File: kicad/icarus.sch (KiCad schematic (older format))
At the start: 78 parts, among them J1 CAN Bus, J2 CAN Bus, J3 SWD Programming, J4 USB_B_Micro, U1 MAX15062A, U10 XT30, U11 XT30, U12 XT30, U13 LT1787HVIMS8PBF, U14 USBLC6-2SC6, U15 STLM20DD9FUDFN-4L_STM-L, U2 STM32G474CEU6, U3 TCAN334G, U4 XT90, U5 FSV10150VTO277-3L_ONS-L, U6 XT30, U7 XT30, U8 TPS2490DGSR, U9 XT30

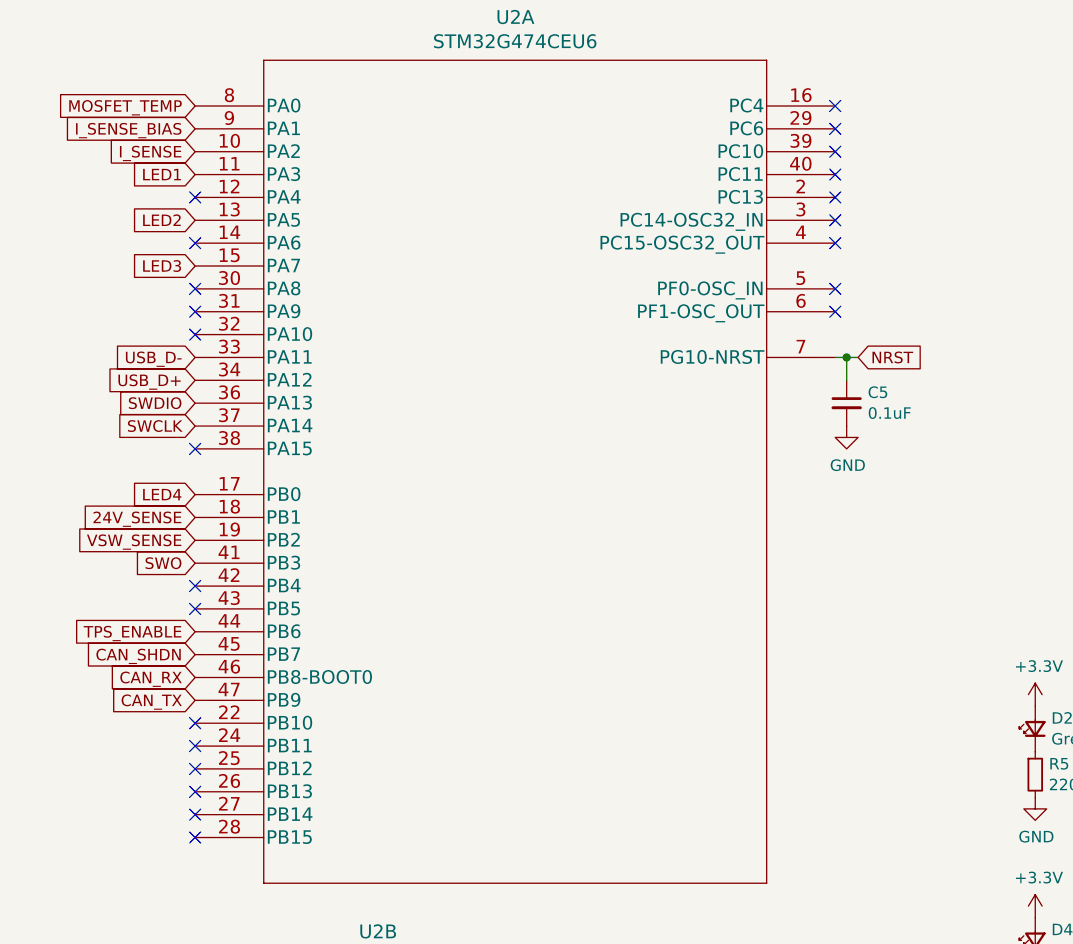
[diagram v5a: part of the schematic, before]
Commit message: Began initial routing
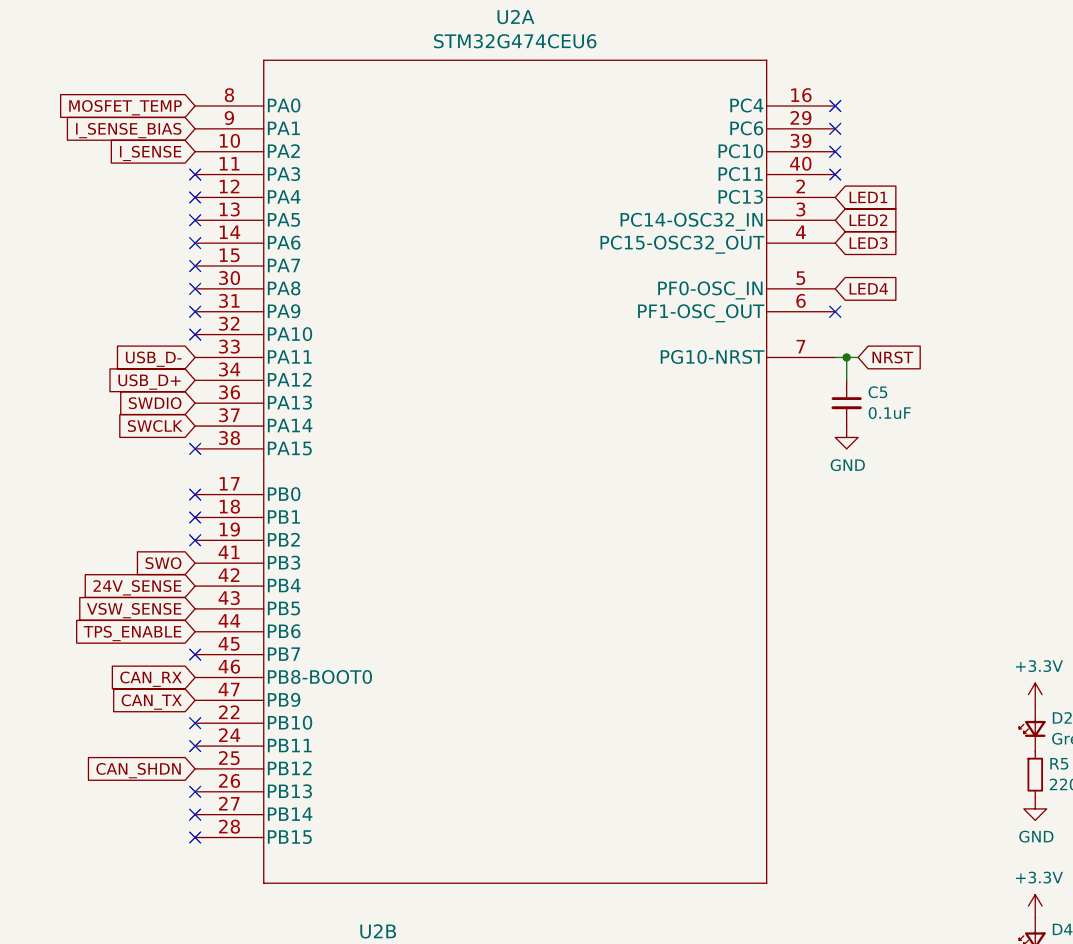
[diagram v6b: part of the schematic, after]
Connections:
- net 24V_SENSE: now also U2.42 (PB4); no longer U2.18 (PB1)
- net CAN_SHDN: now also U2.25 (PB12); no longer U2.45 (PB7)
- net LED1: now also U2.2 (PC13); no longer U2.11 (PA3)
- net LED2: now also U2.3 (PC14-OSC32_IN); no longer U2.13 (PA5)
- net LED3: now also U2.4 (PC15-OSC32_OUT); no longer U2.15 (PA7)
- net LED4: now also U2.5 (PF0-OSC_IN); no longer U2.17 (PB0)
- net VSW_SENSE: now also U2.43 (PB5); no longer U2.19 (PB2)
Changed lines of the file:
@@
 Text GLabel 1250 1625 0    50   Input ~ 0
 I_SENSE_BIAS
-Text GLabel 1250 3925 0    50   Input ~ 0
+Text GLabel 1250 4425 0    50   Input ~ 0
 CAN_SHDN
 $Comp
@@
 Wire Wire Line
 	8175 3525 8350 3525
-Text GLabel 1250 1825 0    50   Input ~ 0
+Text GLabel 4050 1925 2    50   Input ~ 0
 LED1
-Text GLabel 1250 2025 0    50   Input ~ 0
+Text GLabel 4050 2025 2    50   Input ~ 0
 LED2
 Text GLabel 1250 3825 0    50   Input ~ 0
@@
 Text GLabel 5500 6525 0    50   Input ~ 0
 LED4
-Text GLabel 1250 2225 0    50   Input ~ 0
+Text GLabel 4050 2125 2    50   Input ~ 0
 LED3
-Text GLabel 1250 3225 0    50   Input ~ 0
+Text GLabel 4050 2325 2    50   Input ~ 0
 LED4
 Wire Wire Line
@@
 Text GLabel 1250 1725 0    50   Input ~ 0
 I_SENSE
-Text GLabel 1250 3325 0    50   Input ~ 0
+Text GLabel 1250 3625 0    50   Input ~ 0
 24V_SENSE
-Text GLabel 1250 3425 0    50   Input ~ 0
+Text GLabel 1250 3725 0    50   Input ~ 0
 VSW_SENSE
 Text Notes 15425 5400 0    50   ~ 0
@@
 NoConn ~ 1250 2525
 NoConn ~ 1250 3025
-NoConn ~ 1250 3625
-NoConn ~ 1250 3725
 NoConn ~ 1250 4225
 NoConn ~ 1250 4325
-NoConn ~ 1250 4425
 NoConn ~ 1250 4525
 NoConn ~ 1250 4625
 NoConn ~ 1250 4725
 NoConn ~ 4050 2425
-NoConn ~ 4050 2325
-NoConn ~ 4050 2125
-NoConn ~ 4050 2025
-NoConn ~ 4050 1925
 NoConn ~ 4050 1825
 NoConn ~ 4050 1725
@@
 	1    0    0    -1
 $EndComp
+NoConn ~ 1250 3325
+NoConn ~ 1250 3425
+NoConn ~ 1250 3925
+NoConn ~ 1250 1825
+NoConn ~ 1250 2225
+NoConn ~ 1250 2025
+NoConn ~ 1250 3225
 $EndSCHEMATC

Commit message: Added ground plane, adjusted schematic
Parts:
- added JP1: Jumper_2_Bridged, icarus_kicad_lib:SHORT_TOP-BIG, symbol Jumper:Jumper_2_Bridged
- added R18: 6.8k, 1%, Resistor_SMD:R_0402_1005Metric, symbol Device:R_Small
- R17: value R_Small -> 6.8k, 1%
- renumbered R11 to R10, R12 to R11, R13 to R12, R14 to R13, R15 to R14, R2 to R15, R18 to R19, R3 to R2, R19 to R20, R20 to R21, R21 to R22, R4 to R3, R5 to R4, R6 to R5, R7 to R6, R8 to R7, R9 to R8, R10 to R9
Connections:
- net +3V3: now also R15.2
- net +VSW: no longer R15.2
- net GND: now also JP1.1 (A), R18.2; no longer C7.2, CR1.2, CR2.2, U10.-, U11.-, U12.-, U4.-, U5.1 (ANODE), U5.2 (ANODE_2), U6.-, U7.-, U9.-
- net I_SENSE: now also U2.9 (PA1); no longer U2.10 (PA2)
- net I_SENSE_BIAS: now also U2.10 (PA2); no longer U13.6 (VBIAS), U2.9 (PA1)
- net PG: now also U2.19 (PB2)
- net TPS_ENABLE: now also U2.24 (PB11); no longer U2.44 (PB6)
- net at C16.1, R17.2: now also U13.6 (VBIAS), R18.1
- new net GNDPWR: C7.2, CR1.2, CR2.2, JP1.2 (B), U10.-, U11.-, U12.-, U5.1 (ANODE), U5.2 (ANODE_2), U6.-, U7.-, U9.-
- no-connect marks 27 -> 26
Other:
- moved on the sheet: C16, R15

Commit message: Layout v1.0 done
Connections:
- net GND: no longer H2.1, H3.1
- net GNDPWR: now also U4.-
- no-connect marks 26 -> 28
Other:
- moved on the sheet: H2, H3, H4
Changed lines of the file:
@@
 L Mechanical:MountingHole_Pad H2
 U 1 1 604D92AD
+P 13275 6425
+F 0 "H2" V 13229 6575 50  0000 L CNN
+F 1 "MountingHole_Pad" V 13320 6575 50  0000 L CNN
+F 2 "MountingHole:MountingHole_2.7mm_M2.5_DIN965_Pad" H 13275 6425 50  0001 C CNN
+F 3 "~" H 13275 6425 50  0001 C CNN
+	1    13275 6425
+	0    1    1    0
+$EndComp
+$Comp
+L Mechanical:MountingHole_Pad H3
+U 1 1 604D9523
+P 13275 6625
+F 0 "H3" V 13229 6775 50  0000 L CNN
+F 1 "MountingHole_Pad" V 13320 6775 50  0000 L CNN
+F 2 "MountingHole:MountingHole_2.7mm_M2.5_DIN965_Pad" H 13275 6625 50  0001 C CNN
+F 3 "~" H 13275 6625 50  0001 C CNN
+	1    13275 6625
+	0    1    1    0
+$EndComp
+$Comp
+L Mechanical:MountingHole_Pad H4
+U 1 1 604D96CD
 P 13275 5975
-F 0 "H2" V 13229 6125 50  0000 L CNN
+F 0 "H4" V 13229 6125 50  0000 L CNN
 F 1 "MountingHole_Pad" V 13320 6125 50  0000 L CNN
 F 2 "MountingHole:MountingHole_2.7mm_M2.5_DIN965_Pad" H 13275 5975 50  0001 C CNN
@@
 $EndComp
 $Comp
-L Mechanical:MountingHole_Pad H3
-U 1 1 604D9523
-P 13275 6225
-F 0 "H3" V 13229 6375 50  0000 L CNN
-F 1 "MountingHole_Pad" V 13320 6375 50  0000 L CNN
-F 2 "MountingHole:MountingHole_2.7mm_M2.5_DIN965_Pad" H 13275 6225 50  0001 C CNN
-F 3 "~" H 13275 6225 50  0001 C CNN
-	1    13275 6225
-	0    1    1    0
-$EndComp
-$Comp
-L Mechanical:MountingHole_Pad H4
-U 1 1 604D96CD
-P 13275 6475
-F 0 "H4" V 13229 6625 50  0000 L CNN
-F 1 "MountingHole_Pad" V 13320 6625 50  0000 L CNN
-F 2 "MountingHole:MountingHole_2.7mm_M2.5_DIN965_Pad" H 13275 6475 50  0001 C CNN
-F 3 "~" H 13275 6475 50  0001 C CNN
-	1    13275 6475
-	0    1    1    0
-$EndComp
-$Comp
 L power:GND #PWR040
 U 1 1 604DA2B5
-P 13175 6600
-F 0 "#PWR040" H 13175 6350 50  0001 C CNN
-F 1 "GND" H 13180 6427 50  0000 C CNN
-F 2 "" H 13175 6600 50  0001 C CNN
-F 3 "" H 13175 6600 50  0001 C CNN
-	1    13175 6600
+P 13175 5975
+F 0 "#PWR040" H 13175 5725 50  0001 C CNN
+F 1 "GND" H 13180 5802 50  0000 C CNN
+F 2 "" H 13175 5975 50  0001 C CNN
+F 3 "" H 13175 5975 50  0001 C CNN
+	1    13175 5975
 	1    0    0    -1
 $EndComp
 Wire Wire Line
 	13175 5750 13175 5975
-Connection ~ 13175 5975
-Wire Wire Line
-	13175 5975 13175 6225
-Connection ~ 13175 6225
-Wire Wire Line
-	13175 6225 13175 6475
-Connection ~ 13175 6475
-Wire Wire Line
-	13175 6475 13175 6600
 $Comp
 L xt30:XT30 U6
@@
 Connection ~ 11625 3800
 $Comp
-L power:GNDPWR #PWR?
+L power:GNDPWR #PWR0105
 U 1 1 607A32D5
 P 11125 5600
-F 0 "#PWR?" H 11125 5400 50  0001 C CNN
+F 0 "#PWR0105" H 11125 5400 50  0001 C CNN
 F 1 "GNDPWR" H 11129 5446 50  0000 C CNN
 F 2 "" H 11125 5550 50  0001 C CNN
@@
 	1    0    0    -1
 $EndComp
+$Comp
+L power:GNDPWR #PWR0106
+U 1 1 607F4367
+P 15075 4875
+F 0 "#PWR0106" H 15075 4675 50  0001 C CNN
+F 1 "GNDPWR" H 15079 4721 50  0000 C CNN
+F 2 "" H 15075 4825 50  0001 C CNN
+F 3 "" H 15075 4825 50  0001 C CNN
+	1    15075 4875
+	1    0    0    -1
+$EndComp
+Connection ~ 13175 5975
+NoConn ~ 13175 6425
+NoConn ~ 13175 6625
 $EndSCHEMATC
